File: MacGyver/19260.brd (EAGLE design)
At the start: 110.5 x 72.4 mm, 127 parts, among them J1 PST1,0/2-3,5, J10 RJ45J, J13 S04B, J2 PPPC101LFBN, J3 PPPC101LFBN, J4 PPPC101LFBN, J7 Pi Zero, J8 PST1,0/3-3,5, J9 RJ45J, Q1 IRFR5305, Q10 K38, Q11 K38, Q2 K1N, Q201 K1N, Q202 K1N, Q203 K1N, Q3 IRFR5305, Q4 P65, Q5 K3N, Q6 K1N, Q7 K3N, Q8 P65, Q9 K38, U1 1087, U2 1087, U201 74LVC07A, U202 74LVC07A, U203 THVD1500, U204 THVD1500, U205 THVD1500, U206 ATMEGA328PB-AU, U3 I50115, U4 I50115, U5 AVR128DA28-I/SP, Y201 12MHz

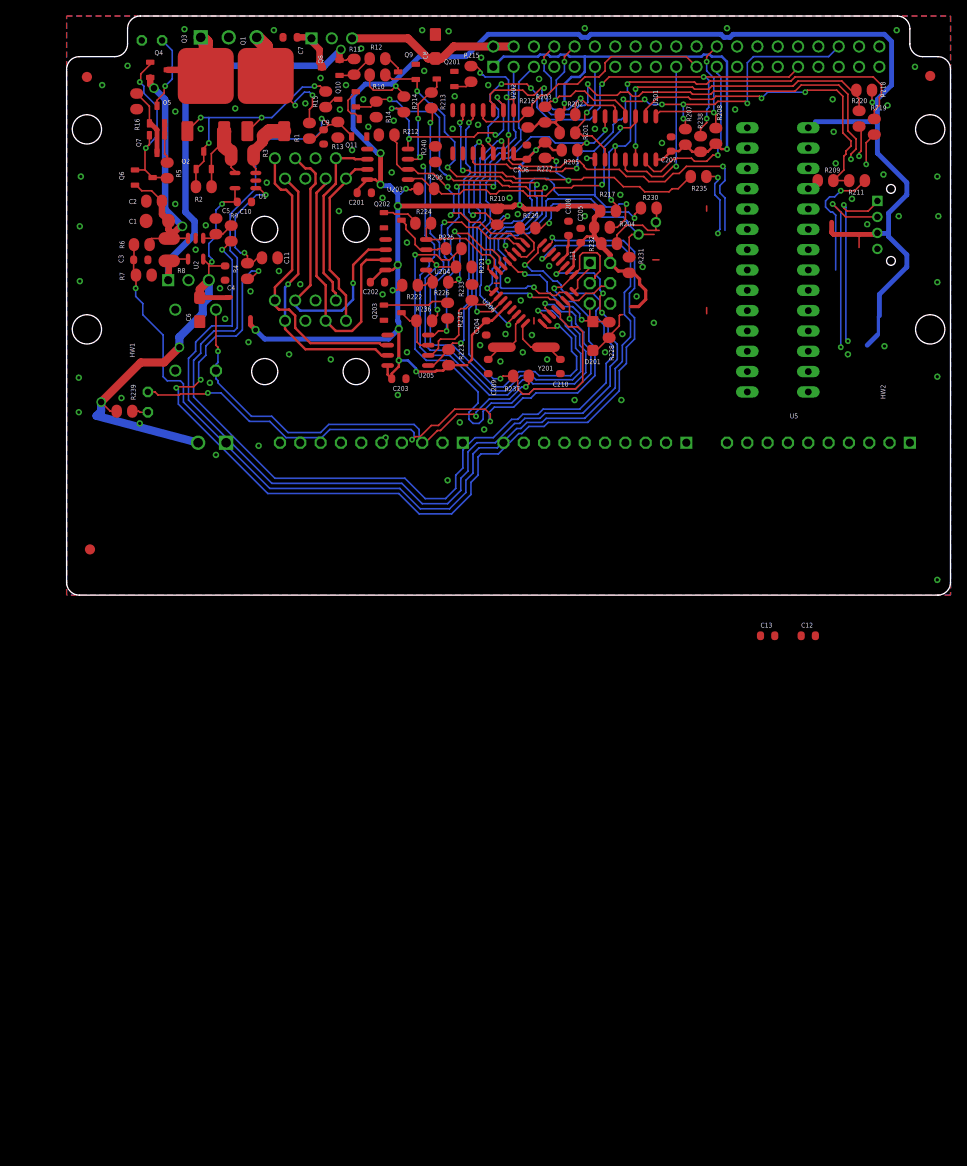
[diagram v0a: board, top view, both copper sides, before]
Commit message: MacGyger: manager will be avr-db, remove spi
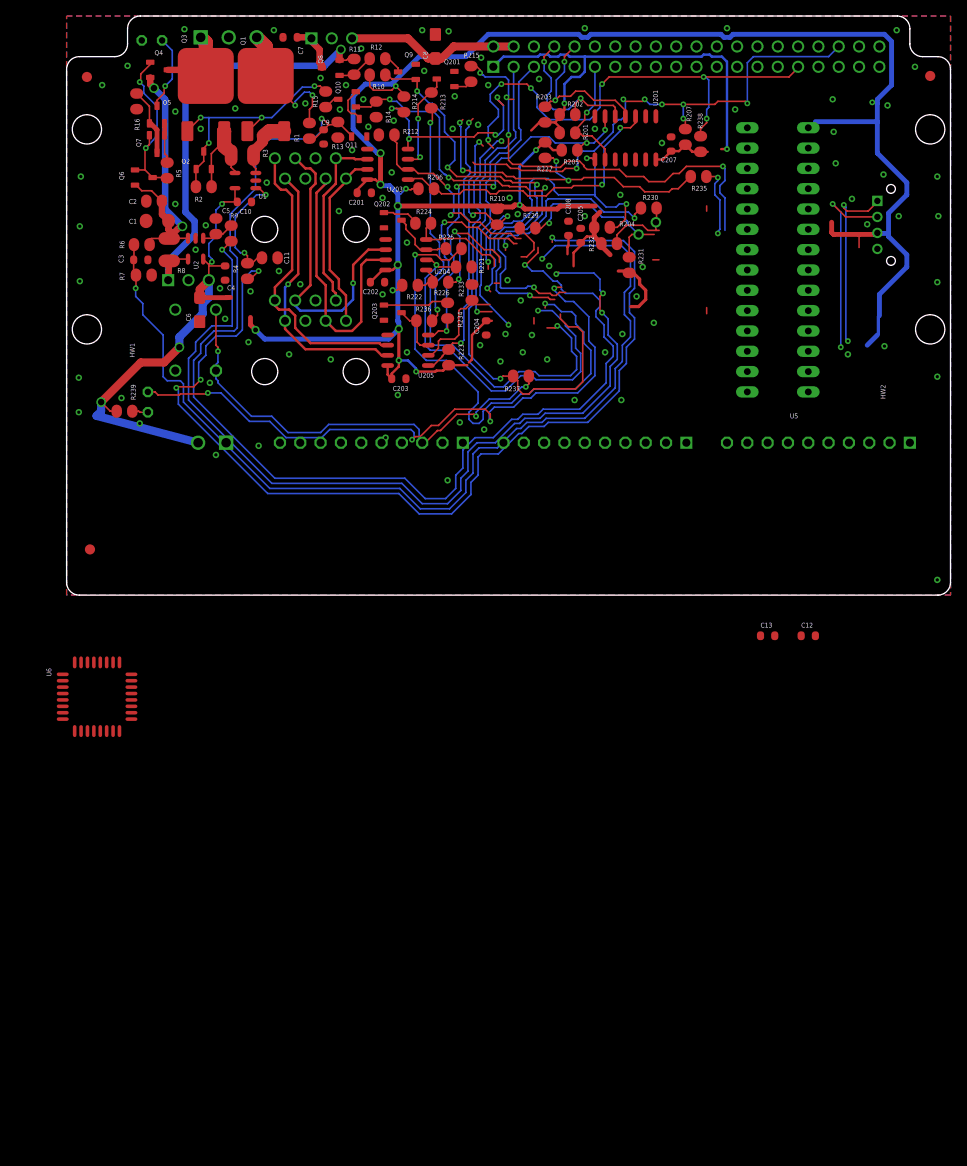
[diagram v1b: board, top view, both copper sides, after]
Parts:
- removed C206: .1uF, C-C:C0603(1608)
- removed C209, C210: 27pF, C-C:C0603(1608)
- removed D201: T4, D-GP:SOD123
- removed J11: (no value), U-AVR:ISP
- removed R208, R240: 10k, R-C:C0805(2012)
- removed R209, R217, R218: 3.01k, R-C:C0805(2012)
- removed R211, R219, R220: 182, R-C:C0805(2012)
- removed R216: 1.82k, R-C:C0805(2012)
- removed R228: 10K, R-C:C0805(2012)
- removed U202: 74LVC07A, U-7400:14SOIC
- removed U206: ATMEGA328PB-AU, U-AVR:TQFP32-08
- removed Y201: 12MHz, Y-XTL:CSM-3X
- added U6: AVR128DB32-I/PT, U-AVR:TQFP32-08
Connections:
- net +DTR renamed +OOB
- net -DTR renamed -OOB
- removed net !RESET!: U202.8
- removed net DTR_!RE: R221.2, U204.2, U206.10
- removed net DTR_DE: R225.2, U206.11
- removed net DTR_RXD: R226.2, U206.30
- removed net DTR_TXD: R224.2, U204.4, U206.31
- removed net ICP3/MOSI: R219.1
- removed net MGR_!RESET: D201.A, J11.5, R228.1, U206.29
- removed net MGR_!SS!: R240.1, U206.14
- removed net MGR_AREF: C208.1, U206.20
- removed net MGR_MISO: J11.1, U206.16
- removed net MGR_SCK: D202.K, J11.3, U206.17
- removed net N$78: R227.2, R235.2, U202.6
- removed net N$88: R240.2, U202.9
- removed net N$91: R218.2, R220.2, U201.12
- removed net N$92: R217.2, R219.2, U201.10
- removed net N$94: R229.2, U206.27
- removed net N$95: R230.2, U206.28
- removed net N$96: R209.2, R211.2, U201.2
- removed net PI_!CS: J7.24, R208.1, U201.1
- removed net PI_MISO: J7.21, R216.2, U202.4
- removed net PI_MOSI: J7.19, U201.11
- removed net PI_SCK: J7.23, U201.13
- removed net SCL1: J7.5, U206.6
- removed net SDA1: J7.3, U206.3
- removed net TX_RPU: R214.2, U202.2, U203.4
- removed net XTAL1: C209.1, U206.7, Y201.1
- removed net XTAL2: C210.1, U206.8, Y201.2
- new net MGR_LED: C208.1, D202.K, U6.17
- new net MGR_SCL0: J7.5, U6.9
- new net MGR_SCL1: R230.2, U6.23
- new net MGR_SDA0: J7.3, U6.8
- new net MGR_SDA1: R229.2, U6.22
- new net MGR_UPDI: U6.27
- new net OOB_!RE: R221.2, U204.2, U6.4
- new net OOB_DE: R225.2, U6.5
- new net OOB_RX2: R226.2, U6.21
- new net OOB_TX2: R224.2, U204.4, U6.20
- new net PI_TX: U6.7
- net !SS: no longer R211.1
- net +5V: now also U6.18, U6.28; no longer C206.1, D201.C, J11.2, R209.1, R217.1, R218.1, R228.2, U202.14, U206.18, U206.4
- net 0V: now also U201.1, U6.19, U6.29; no longer C206.2, C209.2, C210.2, J11.6, U202.7, U206.21, U206.5
- net ALT_EN: now also U6.15; no longer J11.4, U206.15
- net ALT_I: now also U6.11; no longer U206.23
- net ALT_V: now also U6.12; no longer U206.24
- net HOST_!CTS: now also U201.11, U6.32; no longer U202.11, U206.32
- net HOST_!RTS: now also U6.1; no longer U206.1
- net MISO: no longer U202.3
- net PI3V3: now also U6.10; no longer R208.2, R216.1
- net PIPWR_EN: now also U6.16; no longer U206.13
- net PI_!CTS: now also U201.10; no longer U202.10
- net PI_RX: now also U6.6
- net PWR_I: now also U6.13; no longer U206.19
- net PWR_V: now also U6.14; no longer U206.22
- net RX_!RE: now also U6.2; no longer U206.2
- net RX_DE: now also U6.24; no longer U206.26
- net RX_RPU: now also R227.2, R235.2; no longer U202.5
- net SCK: no longer R220.1
- net SHUTDOWN: now also U201.12; no longer U202.12
- net SHUTDWN: now also U201.13, U6.26; no longer U202.13, U206.12
- net TX0: now also R214.2, U203.4; no longer U202.1
- net TX_!RE: now also U6.25; no longer U206.25
- net TX_DE: now also U6.3; no longer U206.9
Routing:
- net MGR_SCK: track 92.6 -> 0.00 mm, vias 4 -> 0
- net MGR_LED: track 0.00 -> 83.3 mm, vias 0 -> 4
- net DTR_DE: track 65.2 -> 0.00 mm, vias 2 -> 0
- net MISO: track 64.8 -> 0.00 mm, vias 3 -> 0
- net OOB_DE: track 0.00 -> 64.1 mm, vias 0 -> 2
- net MGR_!SS!: track 58.7 -> 0.00 mm, vias 2 -> 0
- net N$92: track 57.5 -> 0.00 mm, vias 3 -> 0
- net DTR_!RE: track 50.3 -> 0.00 mm, vias 2 -> 0
- net OOB_!RE: track 0.00 -> 48.9 mm, vias 0 -> 2
- net N$78: track 43.3 -> 0.00 mm, vias 4 -> 0
- net RX_RPU: track 36.1 -> 77.3 mm, vias 2 -> 6
- net N$96: track 41.1 -> 0.00 mm, vias 2 -> 0
- net N$91: track 40.3 -> 0.00 mm, vias 2 -> 0
- net SCL1: track 39.4 -> 0.00 mm, vias 1 -> 0
- net MGR_SCL0: track 0.00 -> 38.0 mm, vias 0 -> 1
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
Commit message: MacGyver: remove rts/cts since no bootloader
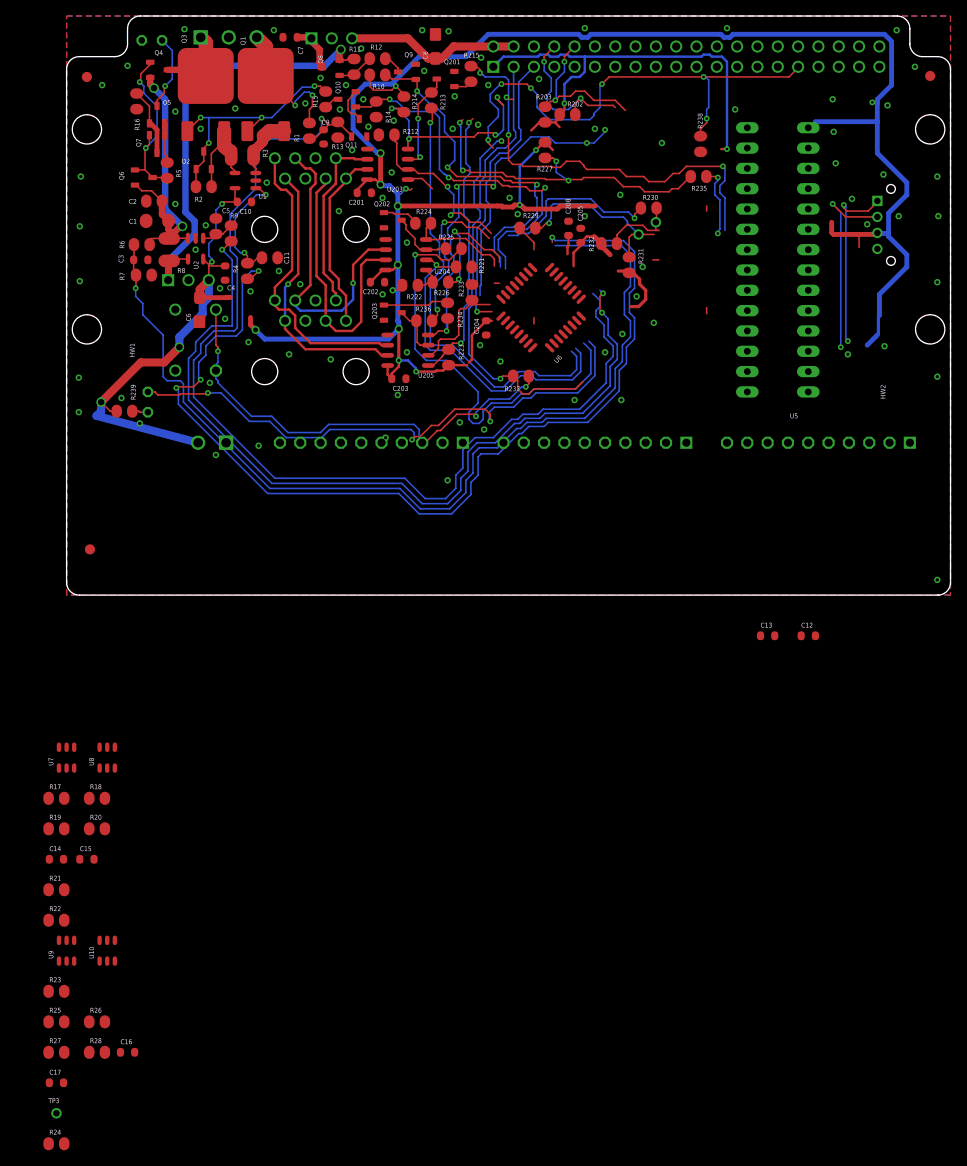
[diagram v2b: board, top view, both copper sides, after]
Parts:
- removed C207: .1uF, C-C:C0603(1608)
- removed R201, R206, R207, R210: 10k, R-C:C0805(2012)
- removed R204, R205: 3.01k, R-C:C0805(2012)
- removed U201: 74LVC07A, U-7400:14SOIC
- added C14, C15, C16, C17: .1uF, C-C:C0603(1608)
- added R17, R19, R20, R23, R24, R25, R26: 3.01k, R-C:C0805(2012)
- added R18: 1.82k, R-C:C0805(2012)
- added R21, R22, R27, R28: 10k, R-C:C0805(2012)
- added TP3: TPPAD1-08, J-TP:P1-08
- added U10, U7, U8, U9: Z4, U-7400:SOT23-6,SOT26
- R238: value 10K -> 100K
- R3: value 0.018 -> 0.010
- moved U6 73.8 mm to (60.6, 35.9), turned to 135 degrees
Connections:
- net MGR_SCL0 renamed SMBUS_SCL
- net MGR_SCL1 renamed I2C_SCL_
- net MGR_SDA0 renamed SMBUS_SDA
- net MGR_SDA1 renamed I2C_SDA_
- net OOB_RX2 renamed FROM_RPU_OOB
- net OOB_TX2 renamed TO_RPU_OOB
- net SCL0 renamed I2C_SCL
- net SDA0 renamed I2C_SDA
- removed net HOST_!CTS: R210.1, U201.11, U6.32
- removed net HOST_!RTS: R204.1, U201.8, U6.1
- removed net HOST_RX: R206.1, U201.3, U203.1
- removed net HOST_TX: R205.1, R234.1, U201.6, U205.4
- removed net N$89: J7.8, R202.2, U201.5
- removed net N$90: J7.11, R201.2, U201.9
- removed net PI_!CTS: J7.36, R207.1, U201.10
- removed net PI_RX: J7.10, R203.1, U201.4, U6.6
- removed net PI_TX: U6.7
- removed net RX0: J4.7, R235.1, U5.23
- removed net SHUTDOWN: J7.31, R238.1, U201.12
- removed net TX0: J4.6, R214.2, R215.2, U203.4, U5.22
- removed net UART_: J7.16
- removed net UPDI_: J7.18
- new net APP_RX0: J4.7, R23.2, U5.23, U9.6
- new net APP_TX0: J4.6, U5.22, U9.3
- new net APP_UART_: C16.1, R27.1, U6.32, U9.5
- new net APP_UPDI_: C17.1, R28.1, U10.5, U6.1
- new net FROM_RPU_RX: R235.1, U10.1, U9.1
- new net FROM_RPU_TX: U203.1, U7.3
- new net N$1: R19.2, R20.2, U8.6
- new net N$11: U6.30
- new net N$3: R25.2, R26.2, U10.6
- new net N$9: U6.31
- new net PI_RX0: J7.10, R18.2, R203.1, U6.6, U7.4, U8.4
- new net PI_TX0: J7.8, R202.2, U6.7, U7.1, U8.1
- new net PI_UART_TO_MGR_UPDI: C15.1, J7.18, R22.1, U8.5
- new net PI_UART_TO_RPU: C14.1, J7.16, R21.1, U7.5
- new net SHUTDWN_TO_BCM6: J7.31, R238.1
- new net TO_RPU_RX: R17.2, R234.1, U205.4, U7.6
- new net TO_RPU_TX: R214.2, R215.2, R24.2, U10.4, U203.4, U9.4
- net +5V: now also R17.1, R19.1, R23.1, R24.1, R25.1; no longer R204.2, R205.2, R206.2, R210.2
- net 0V: now also C14.2, C15.2, C16.2, C17.2, R21.2, R22.2, R27.2, R28.2, U10.2, U7.2, U8.2, U9.2; no longer C207.2, U201.1, U201.7
- net MGR_UPDI: now also R20.1, TP3.TP, U8.3
- net PI3V3: now also R18.1; no longer C207.1, R201.1, R207.2, R238.2, U201.14
- net SHUTDWN: now also R238.2; no longer U201.13
- net UPDI-APP: now also R26.1, U10.3
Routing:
- net TX0: track 81.4 -> 0.00 mm, vias 8 -> 0
- net TO_RPU_TX: track 0.00 -> 81.4 mm, vias 0 -> 8
- net PI_!CTS: track 62.7 -> 0.00 mm, vias 7 -> 0
- net SHUTDWN_TO_BCM6: track 0.00 -> 62.5 mm, vias 0 -> 6
- net SHUTDOWN: track 62.5 -> 0.00 mm, vias 6 -> 0
- net HOST_TX: track 50.7 -> 0.00 mm, vias 5 -> 0
- net TO_RPU_RX: track 0.00 -> 47.7 mm, vias 0 -> 5
- net HOST_!RTS: track 43.2 -> 0.00 mm, vias 3 -> 0
- net HOST_RX: track 37.8 -> 0.00 mm, vias 2 -> 0
- net HOST_!CTS: track 24.3 -> 0.00 mm, vias 4 -> 0
- net N$89: track 21.5 -> 0.00 mm, vias 2 -> 0
- net PI_TX0: track 0.00 -> 20.4 mm, vias 0 -> 2
- net PI_RX: track 20.3 -> 0.00 mm, vias 2 -> 0
- net PI_RX0: track 0.00 -> 19.6 mm, vias 0 -> 2
- net N$90: track 15.1 -> 0.00 mm, vias 1 -> 0
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
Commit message: MacGyver: starting layout
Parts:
- removed C16, C17, C205, C208: .1uF, C-C:C0603(1608)
- removed J13: S04B, J-HDR2mm:B04B
- removed R202, R27, R28: 10k, R-C:C0805(2012)
- removed R203: 1.82k, R-C:C0805(2012)
- removed R227: 10K, R-C:C0805(2012)
- removed R229, R230, R235: 182, R-C:C0805(2012)
- removed R23, R231, R232, R24, R25, R26: 3.01k, R-C:C0805(2012)
- removed R238: 100K, R-C:C0805(2012)
- removed U10, U8, U9: Z4, U-7400:SOT23-6,SOT26
- added C103, C104, C107, C110: .1uF, C-C:C0603(1608)
- added C108, C109: 27pF, C-C:C0603(1608)
- added J5: Pi Zero, U-Pi:RASPI_ZERO_V40PIN
- added R101, R117, R118: 10k, R-C:C0805(2012)
- added R102, R105, R106, R126, R127: 3.01k, R-C:C0805(2012)
- added R103: 1.82k, R-C:C0805(2012)
- added R115: 100K, R-C:C0805(2012)
- added R122, R124, R125: 182, R-C:C0805(2012)
- added U101, U103: Z4, U-7400:SOT23-6,SOT26
- added U106: AVR128DB32-I/PT, U-AVR:TQFP32-08
- added Y1: 16MHz, Y-XTL:CSM-3X
- J7: value Pi Zero -> S04B; device U-Pi:RASPI_ZERO_V40PIN -> J-HDR2mm:B04B
- Q2: value K1N -> IRFR5305; device Q-NPN:SOT23 -> Q-PCH:DPAK
- Q3: value IRFR5305 -> P65; device Q-PCH:DPAK -> Q-PCH:SOT23
- Q4: value P65 -> K3N; device Q-PCH:SOT23 -> Q-PNP:SOT23
- Q5: value K3N -> K1N; device Q-PNP:SOT23 -> Q-NPN:SOT23
- Q6: value K1N -> K3N; device Q-NPN:SOT23 -> Q-PNP:SOT23
- Q7: value K3N -> P65; device Q-PNP:SOT23 -> Q-PCH:SOT23
- Q8: value P65 -> K38; device Q-PCH:SOT23 -> Q-NCH:SOT23
- Q9: value K38 -> K1N; device Q-NCH:SOT23 -> Q-NPN:SOT23
- R10: value 10k -> 80.6k
- R11: value 100k -> 10k
- R12: value 80.6k -> 100k
- R14: value 10k -> 49.9k
- R15: value 49.9k -> 10k
- R18: value 1.82k -> 10k
- R2: value 100k -> 0.010; device R-C:C0805(2012) -> R-C:C1210(3225)
- R21: value 10k -> 3.01k
- R3: value 0.010 -> 1K; device R-C:C1210(3225) -> R-C:C0805(2012)
- R4, R9: value 10k -> 100k
- R5: value 1K -> 15.8k
- R6: value 100k -> 0.068; device R-C:C0805(2012) -> R-C:C1210(3225)
- R7: value 15.8k -> 10k
- R8: value 0.068 -> 10k; device R-C:C1210(3225) -> R-C:C0805(2012)
- U5: value AVR128DA28-I/SP -> Z4; device U-AVR:DIL28-3 -> U-7400:SOT23-6,SOT26
- U6: value AVR128DB32-I/PT -> AVR128DA28-I/SP; device U-AVR:TQFP32-08 -> U-AVR:DIL28-3
- moved U5 123.9 mm to (1.27, -44.5), turned to 0 degrees
- moved C12 99.8 mm to (8.89, -57.1)
- moved C14 93.2 mm to (88.9, -5.08)
- moved J2 55.9 mm to (50.8, 19.1)
- moved J7 51.7 mm to (102.6, 49.3), turned to 270 degrees
- moved R19 39.4 mm to (0.00, -68.6)
- moved R8 34.0 mm to (40.1, 65.0), turned to 180 degrees
- moved R18 32.2 mm to (0.00, -57.1)
- moved U6 30.2 mm to (90.2, 41.9), turned to 90 degrees
- moved C15 28.2 mm to (0.00, -61.0)
- moved J4 27.9 mm to (106.7, 19.1)
- moved J3 27.9 mm to (78.7, 19.1)
- moved Q9 27.7 mm to (18.4, 54.4), turned to 0 degrees
- moved R12 27.0 mm to (18.4, 51.1)
- moved R9 25.9 mm to (37.2, 66.0), turned to 270 degrees
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- renumbered C201 to C101, C202 to C102, C203 to C105, C204 to C106, D2 to D1, D202 to D101, J8 to J6, Q201 to Q101, Q202 to Q102, Q203 to Q103, R212 to R108, R213 to R110, R214 to R104, R215 to R114, R221 to R107, R222 to R109, R223 to R120, R224 to R112, R225 to R111, R226 to R113, R233 to R119, R234 to R121, R236 to R123, R237 to R116, R239 to R128, U203 to U102, U204 to U104, U205 to U105
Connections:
- removed net PI_RX0: J7.10, R18.2, R203.1, U6.6, U7.4, U8.4
- removed net PI_TX0: J7.8, R202.2, U6.7, U7.1, U8.1
- removed net UPDI-APP: J4.8, R26.1, U10.3, U5.19
- new net APP_UPDI: J3.8, R21.1, U6.19, U7.3
- new net PI_RX: J5.10, R103.2, U101.4, U103.4, U106.6
- new net PI_TX: J5.8, R101.2, U101.1, U103.1, U106.7
- net !RESET: now also J3.5, U6.18; no longer J4.5, U5.18
- net !SS: now also J2.8, U6.1; no longer J3.8, U5.1
- net +5V: now also C107.1, C14.1, J7.3, R102.1, R105.1, R126.2, R127.2, R20.1, R8.2, U106.18, U106.28, U6.14, U6.20; no longer C12.1, C205.1, J13.3, R10.2, R227.1, R23.1, R231.2, R232.2, R24.1, R25.1, U5.14, U5.20, U6.18, U6.28
- net +5V_2PI: now also J5.2, J5.4; no longer J7.2, J7.4
- net 0V: now also C103.2, C104.2, C107.2, C108.1, C109.1, C110.2, J5.14, J5.20, J5.25, J5.30, J5.34, J5.39, J5.6, J5.9, J7.4, Q8.2(S), R11.1, R117.2, R118.2, R13.2, R18.2, R5.1, U101.2, U103.2, U106.19, U106.29, U5.2, U6.15, U6.21; no longer C16.2, C17.2, C205.2, C208.2, J13.4, J7.14, J7.20, J7.25, J7.30, J7.34, J7.39, J7.6, J7.9, Q9.2(S), R13.1, R14.2, R21.2, R27.2, R28.2, R7.1, U10.2, U5.15, U5.21, U6.19, U6.29, U8.2, U9.2
- net AIN0: now also J4.3, U6.6; no longer J2.3, U5.6
- net AIN1: now also J4.4, U6.7; no longer J2.4, U5.7
- net AIN2: now also J4.5, U6.8; no longer J2.5, U5.8
- net AIN3: now also J4.6, U6.9; no longer J2.6, U5.9
- net AIN4: now also J4.7, U6.10; no longer J2.7, U5.10
- net AIN5: now also J4.8, U6.11; no longer J2.8, U5.11
- net AIN6: now also J4.9, U6.12; no longer J2.9, U5.12
- net AIN7: now also J4.10, U6.13; no longer J2.10, U5.13
- net ALT_EN: now also R13.1, U106.15; no longer R14.1, U6.15
- net ALT_I: now also R15.1, U106.11; no longer R4.1, U6.11
- net ALT_V: now also R11.2, U106.12; no longer R13.2, U6.12
- net APP_RX0: now also J3.7, R17.2, U5.6, U6.23; no longer J4.7, R23.2, U5.23, U9.6
- net APP_TX0: now also J3.6, U5.3, U6.22; no longer J4.6, U5.22, U9.3
- net APP_UART_: now also C12.1, R18.1, U106.32, U5.5; no longer C16.1, R27.1, U6.32, U9.5
- net APP_UPDI_: now also C15.1, R22.1, U106.1, U7.5; no longer C17.1, R28.1, U10.5, U6.1
- net FROM_RPU_OOB: now also U106.21; no longer U6.21
- net FROM_RPU_RX: now also R122.1, U5.1, U7.1; no longer R235.1, U10.1, U9.1
- net FROM_RPU_TX: now also U101.3; no longer U7.3
- net I2C_SCL: now also J2.4, J7.1, R125.1, R127.1, U6.25; no longer J13.1, J3.4, R230.1, R232.1, U5.25
- net I2C_SCL_: now also R125.2, U106.23; no longer R230.2, U6.23
- net I2C_SDA: now also J2.3, J7.2, R124.1, R126.1, U6.24; no longer J13.2, J3.3, R229.1, R231.1, U5.24
- net I2C_SDA_: now also R124.2, U106.22; no longer R229.2, U6.22
- net MGR_LED: now also C110.1, U106.17; no longer C208.1, U6.17
- net MGR_UPDI: now also R106.1, U103.3, U106.27; no longer R20.1, U6.27, U8.3
- net MISO: now also J2.6, U6.27; no longer J3.6, U5.27
- net MOSI: now also J2.5, U6.26; no longer J3.5, U5.26
- net N$1: now also R105.2, R106.2, U103.6; no longer R19.2, R20.2, U8.6
- net N$10: now also Q4.E, Q6.B, R3.1; no longer Q5.E, Q7.B, R5.1
- net N$11: now also C109.2, U106.30, Y1.2; no longer U6.30
- net N$2: now also Q7.1(G), R10.1, R9.2; no longer Q8.1(G), R11.2, R12.1
- net N$3: now also R20.2, R21.2, U7.6; no longer R25.2, R26.2, U10.6
- net N$32: now also Q2.3, Q9.E, R12.2, R2.1; no longer Q2.E, Q3.3, R2.2, R3.1
- net N$33: now also Q2.1, Q9.B, Q9.C, R12.1, R14.2; no longer Q2.B, Q2.C, Q3.1, R15.2, R2.1
- net N$34: now also R14.1; no longer R15.1
- net N$4: now also Q8.3(D), R10.2; no longer Q9.3(D), R12.2
- net N$5: now also Q4.B, Q6.C; no longer Q5.B, Q7.C
- net N$6: now also Q3.1(G), Q5.B, Q5.C, Q6.E, R3.2; no longer Q4.1(G), Q6.B, Q6.C, Q7.E, R5.2
- net N$65: now also R15.2; no longer R4.2
- net N$66: now also R2.2; no longer R3.2
- net N$7: now also Q4.C; no longer Q5.C
- net N$8: now also R7.2; no longer R9.2
- net N$9: now also C108.2, U106.31, Y1.1; no longer U6.31
- net OOB_!RE: now also U106.4; no longer U6.4
- net OOB_DE: now also U106.5; no longer U6.5
- net PC2: now also J3.9, U6.4; no longer J4.9, U5.4
- net PC3: now also J3.10, U6.5; no longer J4.10, U5.5
- net PI3V3: now also J5.1, R101.1, R103.1, U106.10; no longer J7.1, R18.1, R202.1, R203.2, U6.10
- net PIPWR_EN: now also Q8.1(G), R8.1, U106.16; no longer Q9.1(G), R10.1, U6.16
- net PI_UART_TO_MGR_UPDI: now also C104.1, J5.18, R118.1, U103.5; no longer C15.1, J7.18, R22.1, U8.5
- net PI_UART_TO_RPU: now also C103.1, J5.16, R117.1, U101.5; no longer C14.1, J7.16, R21.1, U7.5
- net POWER: now also Q2.SINK, Q3.3(D); no longer Q3.SINK, Q4.3(D)
- net PWR_I: now also R7.1, U106.13; no longer R9.1, U6.13
- net PWR_V: now also R4.1, R5.2, U106.14; no longer R6.1, R7.2, U6.14
- net RX1: now also J2.10, U6.3; no longer J3.10, U5.3
- net RX2: now also J3.4, U6.17; no longer J4.4, U5.17
- net RX_!RE: now also U106.2; no longer U6.2
- net RX_DE: now also U106.24; no longer U6.24
- net RX_RPU: now also R122.2; no longer R227.2, R235.2
- net SCK: now also J2.7, U6.28; no longer J3.7, U5.28
- net SHLD_VIN: now also Q7.3(D); no longer Q8.3(D)
- net SHUTDWN: now also R115.2, U106.26; no longer R238.2, U6.26
- net SHUTDWN_TO_BCM6: now also J5.31, R115.1; no longer J7.31, R238.1
- net SMBUS_SCL: now also J5.5, U106.9; no longer J7.5, U6.9
- net SMBUS_SDA: now also J5.3, U106.8; no longer J7.3, U6.8
- net TO_RPU_OOB: now also U106.20; no longer U6.20
- net TO_RPU_RX: now also R102.2, U101.6; no longer R17.2, U7.6
- net TO_RPU_TX: now also R19.2, U5.4, U7.4; no longer R24.2, U10.4, U9.4
- net TX1: now also J2.9, U6.2; no longer J3.9, U5.2
- net TX2: now also J3.3, U6.16; no longer J4.3, U5.16
- net TX_!RE: now also U106.25; no longer U6.25
- net TX_DE: now also U106.3; no longer U6.3
- net VIN: now also Q7.2(S), R6.1, R9.1; no longer Q8.2(S), R11.1, R8.1
- net VIN_S: now also Q3.2(S), Q5.E, R4.2; no longer Q4.2(S), Q6.E, R8.2
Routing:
- net TO_RPU_TX: track 81.4 -> 8.12 mm, vias 8 -> 2
- net SHUTDWN_TO_BCM6: track 62.5 -> 0.00 mm, vias 6 -> 0
- net +5V: track 349.4 -> 287.7 mm, vias 18 -> 16
- net OOB_DE: track 55.2 -> 0.00 mm, vias 1 -> 0
- net TX_DE: track 55.3 -> 0.18 mm, vias 1 -> 0
- net RX_RPU: track 77.3 -> 29.1 mm, vias 6 -> 1
- net SHUTDWN: track 47.4 -> 0.00 mm, vias 2 -> 0
- net PI3V3: track 56.9 -> 15.2 mm, vias 2 -> 0
- net OOB_!RE: track 41.1 -> 4.09 mm, vias 1 -> 0
- net SMBUS_SDA: track 35.8 -> 7.87 mm, vias 1 -> 0
- net ALT_EN: track 47.0 -> 20.6 mm, vias 3 -> 2
- net PIPWR_EN: track 44.1 -> 19.3 mm, vias 3 -> 2
- net TO_RPU_RX: track 47.7 -> 23.5 mm, vias 5 -> 1
- net SMBUS_SCL: track 32.6 -> 8.41 mm
- net I2C_SDA: track 47.4 -> 24.6 mm, vias 3 -> 2
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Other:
- board text removed: "REMOVE ALTERNAT POWER BEFOR ISP PROGRAMING"
